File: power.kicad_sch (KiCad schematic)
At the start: 108 parts, among them U41 TPS7A8801RTJR, U42 TPS7A8801RTJR, U43 TPS61252DSG, U44 TPSM863252RDXR, U45 TPS7A3301RGW, U46 TPSM863252RDXR

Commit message: Nearly all routed.  Repinning FDA resistors.
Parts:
- renumbered C461 to C43
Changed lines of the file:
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@@
 		(on_board yes)
 		(dnp no)
-		(property "Reference" "C461"
+		(property "Reference" "C43"
 			(at 156.21 109.982 0)
 			(effects
@@
 			(project "lincal"
 				(path "/b054cef4-39e3-49d8-aff0-7ba5a206c187/98a8b958-69ae-452b-9f02-aef214a697d8"
-					(reference "C461")
+					(reference "C43")
 					(unit 1)
 				)

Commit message: DRC update.  Repin ADC.  De-crack the S/H ground.
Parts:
- U45: footprint Package_DFN_QFN:Texas_RGW0020A_VQFN-20-1EP_5x5mm_P0.65mm_EP3.15x3.15mm -> Parts:Texas_RGW0020A_VQFN-20-1EP_5x5mm_P0.65mm_EP3.15x3.15mm
- renumbered C433 to C40, C42 to C453
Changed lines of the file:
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@@
 			(effects
 				(font
-					(size 1.27 1.27)
-				)
-			)
-		)
-		(property "Footprint" "Package_DFN_QFN:Texas_RGW0020A_VQFN-20-1EP_5x5mm_P0.65mm_EP3.15x3.15mm"
+					(size 1.524 1.524)
+				)
+			)
+		)
+		(property "Footprint" "Parts:Texas_RGW0020A_VQFN-20-1EP_5x5mm_P0.65mm_EP3.15x3.15mm"
 			(at 177.8 96.52 0)
 			(effects
@@
 		(on_board yes)
 		(dnp no)
-		(property "Reference" "C433"
+		(property "Reference" "C40"
 			(at 72.39 146.05 0)
 			(effects
@@
 			(project "lincal"
 				(path "/b054cef4-39e3-49d8-aff0-7ba5a206c187/98a8b958-69ae-452b-9f02-aef214a697d8"
-					(reference "C433")
+					(reference "C40")
 					(unit 1)
 				)
@@
 		(on_board yes)
 		(dnp no)
-		(property "Reference" "C42"
+		(property "Reference" "C453"
 			(at 213.36 69.85 0)
 			(effects
@@
 			(project "lincal"
 				(path "/b054cef4-39e3-49d8-aff0-7ba5a206c187/98a8b958-69ae-452b-9f02-aef214a697d8"
-					(reference "C42")
-					(unit 1)
-				)
+					(reference "C453")
+					(unit 1)
+				)

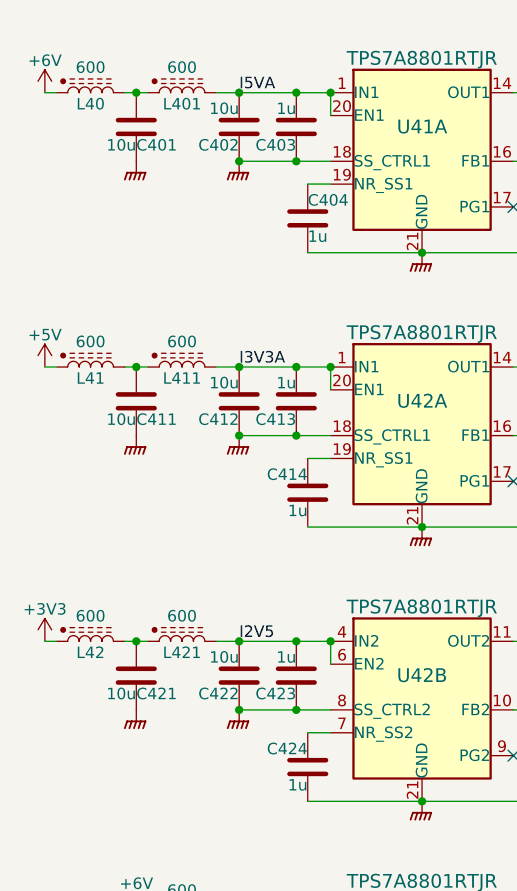
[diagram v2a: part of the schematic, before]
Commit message: Remove placebo planes.  Tidy some analog routing.
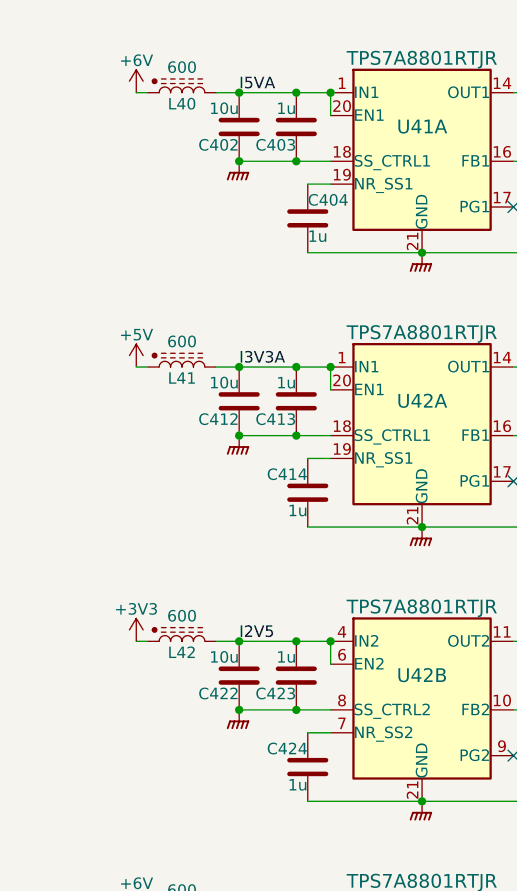
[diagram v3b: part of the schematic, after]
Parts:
- removed C401, C411, C421: 10u, Capacitor_SMD:C_0603_1608Metric, symbol Device:C
- removed L401, L411, L421: 600, Inductor_SMD:L_0603_1608Metric, symbol Parts:L_Ferrite_Power
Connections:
- net I2V5: now also L42.2
- net I3V3A: now also L41.2
- net I5VA: now also L40.2
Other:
- moved on the sheet: L40, L41, L42

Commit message: More component metadata.
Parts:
- C40, C402, C403, C404, C405, C406, C407, C41, C412, C413, C414, C415, C416, C417, C422, C423, C424, C425, C426, C427, C43, C431, C432, C434, C435, C436, C441, C442, C444, C445, C451, C452, C453, C454, C455, C462, C463, C464, C465, C466, C467, C468, C471, C472, C473, C474, C475, C476, D41, D42, D43, L40, L41, L42, L43, L44, L45, L46, L461, L47, R401, R402, R403, R411, R412, R413, R421, R422, R423, R431, R432, R433, R441, R442, R443, R451, R452, R453, R462, R463, R464, R471, R472, R473, R474, R475, U44, U45, U46: Stock (none) -> JLC
- C443: Stock (none) -> DNP
- L441, U43: Stock (none) -> ?
- TP41, TP42, TP43, TP44, TP45, TP46, TP47, TP48: Stock - -> Board

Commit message: Front panel
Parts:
- U41, U42: footprint Package_DFN_QFN:QFN-20-1EP_4x4mm_P0.5mm_EP2.7x2.7mm -> Parts:QFN-20-1EP_4x4mm_P0.5mm_EP2.7x2.7mm
- renumbered TP46 to -2V5, TP45 to 2V5, TP43 to 3V3, TP44 to 3V3A1, TP41 to 5V1, TP47 to 5V6, TP42 to 6V1
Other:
- note removed: "TODO - LM27761 for -3V3 switcher?"
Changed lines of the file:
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@@
 	(generator_version "9.0")
 	(paper "A4")
-	(text "TODO - LM27761 for -3V3 switcher?"
-		(exclude_from_sim no)
-		(at 175.006 151.13 0)
-		(effects
-			(font
-				(size 1.27 1.27)
-			)
-			(justify top)
-		)
-	)
 	(text "Margined to 5.1V"
 		(exclude_from_sim no)
@@
 		(on_board yes)
 		(dnp no)
-		(property "Reference" "TP45"
+		(property "Reference" "2V5"
 			(at 102.87 97.536 0)
 			(effects
@@
 			(project "lincal"
 				(path "/b054cef4-39e3-49d8-aff0-7ba5a206c187/98a8b958-69ae-452b-9f02-aef214a697d8"
-					(reference "TP45")
+					(reference "2V5")
 					(unit 1)
 				)
@@
 			)
 		)
-		(property "Footprint" "Package_DFN_QFN:QFN-20-1EP_4x4mm_P0.5mm_EP2.7x2.7mm"
+		(property "Footprint" "Parts:QFN-20-1EP_4x4mm_P0.5mm_EP2.7x2.7mm"
 			(at 85.09 109.22 0)
 			(effects
@@
 		(on_board yes)
 		(dnp no)
-		(property "Reference" "TP41"
+		(property "Reference" "5V1"
 			(at 102.87 36.576 0)
 			(effects
@@
 			(project "lincal"
 				(path "/b054cef4-39e3-49d8-aff0-7ba5a206c187/98a8b958-69ae-452b-9f02-aef214a697d8"
-					(reference "TP41")
+					(reference "5V1")
 					(unit 1)
 				)
@@
 		(on_board yes)
 		(dnp no)
-		(property "Reference" "TP44"
+		(property "Reference" "3V3A1"
 			(at 102.87 67.056 0)
 			(effects
@@
 			(project "lincal"
 				(path "/b054cef4-39e3-49d8-aff0-7ba5a206c187/98a8b958-69ae-452b-9f02-aef214a697d8"
-					(reference "TP44")
+					(reference "3V3A1")
 					(unit 1)
 				)
@@
 			)
 		)
-		(property "Footprint" "Package_DFN_QFN:QFN-20-1EP_4x4mm_P0.5mm_EP2.7x2.7mm"
+		(property "Footprint" "Parts:QFN-20-1EP_4x4mm_P0.5mm_EP2.7x2.7mm"
 			(at 85.09 48.26 0)
 			(effects
@@
 			)
 		)
-		(property "Footprint" "Package_DFN_QFN:QFN-20-1EP_4x4mm_P0.5mm_EP2.7x2.7mm"
+		(property "Footprint" "Parts:QFN-20-1EP_4x4mm_P0.5mm_EP2.7x2.7mm"
 			(at 85.09 78.74 0)
 			(effects
@@
 		(on_board yes)
 		(dnp no)
-		(property "Reference" "TP46"
+		(property "Reference" "-2V5"
 			(at 219.71 97.536 0)
 			(effects
@@
 			(project "lincal"
 				(path "/b054cef4-39e3-49d8-aff0-7ba5a206c187/98a8b958-69ae-452b-9f02-aef214a697d8"
-					(reference "TP46")
+					(reference "-2V5")
 					(unit 1)
 				)
@@
 		(on_board yes)
 		(dnp no)
-		(property "Reference" "TP47"
+		(property "Reference" "5V6"
 			(at 102.87 128.016 0)
 			(effects
@@
 			(project "lincal"
 				(path "/b054cef4-39e3-49d8-aff0-7ba5a206c187/98a8b958-69ae-452b-9f02-aef214a697d8"
-					(reference "TP47")
+					(reference "5V6")
 					(unit 1)
 				)
@@
 			)
 		)
-		(property "Footprint" "Package_DFN_QFN:QFN-20-1EP_4x4mm_P0.5mm_EP2.7x2.7mm"
+		(property "Footprint" "Parts:QFN-20-1EP_4x4mm_P0.5mm_EP2.7x2.7mm"
 			(at 85.09 139.7 0)
 			(effects
@@
 		(on_board yes)
 		(dnp no)
-		(property "Reference" "TP42"
+		(property "Reference" "6V1"
 			(at 207.01 36.576 0)
 			(effects
@@
 			(project "lincal"
 				(path "/b054cef4-39e3-49d8-aff0-7ba5a206c187/98a8b958-69ae-452b-9f02-aef214a697d8"
-					(reference "TP42")
+					(reference "6V1")
 					(unit 1)
 				)
@@
 		(on_board yes)
 		(dnp no)
-		(property "Reference" "TP43"
+		(property "Reference" "3V3"
 			(at 196.85 65.786 0)
 			(effects
@@
 			(project "lincal"
 				(path "/b054cef4-39e3-49d8-aff0-7ba5a206c187/98a8b958-69ae-452b-9f02-aef214a697d8"
-					(reference "TP43")
+					(reference "3V3")
 					(unit 1)
 				)

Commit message: Tweak various feedback loops.
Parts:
- C443: now left out of the parts list
- L441, U43: Stock ? -> LCSC
- U45: now in the parts list
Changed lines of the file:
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@@
 			)
 		)
-		(property "Stock" "?"
+		(property "Stock" "LCSC"
 			(at 176.53 46.99 0)
 			(effects
@@
 		(unit 1)
 		(exclude_from_sim no)
-		(in_bom yes)
+		(in_bom no)
 		(on_board yes)
 		(dnp yes)
@@
 			)
 		)
-		(property "Stock" "?"
+		(property "Stock" "LCSC"
 			(at 171.45 36.83 90)
 			(effects
@@
 		(unit 1)
 		(exclude_from_sim no)
-		(in_bom no)
+		(in_bom yes)
 		(on_board yes)
 		(dnp no)

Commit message: Readyish
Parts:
- C405, C415, C425, C434, C464: LCSC C307500 -> C389113
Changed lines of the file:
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@@
 			)
 		)
-		(property "Datasheet" "C0G, 25V"
+		(property "Datasheet" "C0G, 50V"
 			(at 99.06 45.72 0)
 			(effects
@@
 			)
 		)
-		(property "LCSC" "C307500"
+		(property "LCSC" "C389113"
 			(at 99.06 45.72 0)
 			(effects
@@
 			)
 		)
-		(property "Datasheet" "C0G, 25V"
+		(property "Datasheet" "C0G, 50V"
 			(at 189.23 106.68 0)
 			(effects
@@
 			)
 		)
-		(property "LCSC" "C307500"
+		(property "LCSC" "C389113"
 			(at 189.23 106.68 0)
 			(effects
@@
 			)
 		)
-		(property "Datasheet" "C0G, 25V"
+		(property "Datasheet" "C0G, 50V"
 			(at 99.06 106.68 0)
 			(effects
@@
 			)
 		)
-		(property "LCSC" "C307500"
+		(property "LCSC" "C389113"
 			(at 99.06 106.68 0)
 			(effects
@@
 			)
 		)
-		(property "Datasheet" "C0G, 25V"
+		(property "Datasheet" "C0G, 50V"
 			(at 99.06 137.16 0)
 			(effects
@@
 			)
 		)
-		(property "LCSC" "C307500"
+		(property "LCSC" "C389113"
 			(at 99.06 137.16 0)
 			(effects
@@
 			)
 		)
-		(property "Datasheet" "C0G, 25V"
+		(property "Datasheet" "C0G, 50V"
 			(at 99.06 76.2 0)
 			(effects
@@
 			)
 		)
-		(property "LCSC" "C307500"
+		(property "LCSC" "C389113"
 			(at 99.06 76.2 0)
 			(effects
